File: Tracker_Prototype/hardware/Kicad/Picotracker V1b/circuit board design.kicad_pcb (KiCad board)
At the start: 2 copper layers, 47.4 x 20.1 mm, 55 parts, among them IC7 SPV1040, J1 Conn_01x06, J2 GND, J3 +SOL, J4 BATT_V+, J5 BATT_GND, J6 ICSS LOGO, Q1 Q_PMOS_DGS, SW1 SW_Push, U2 TPS62740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

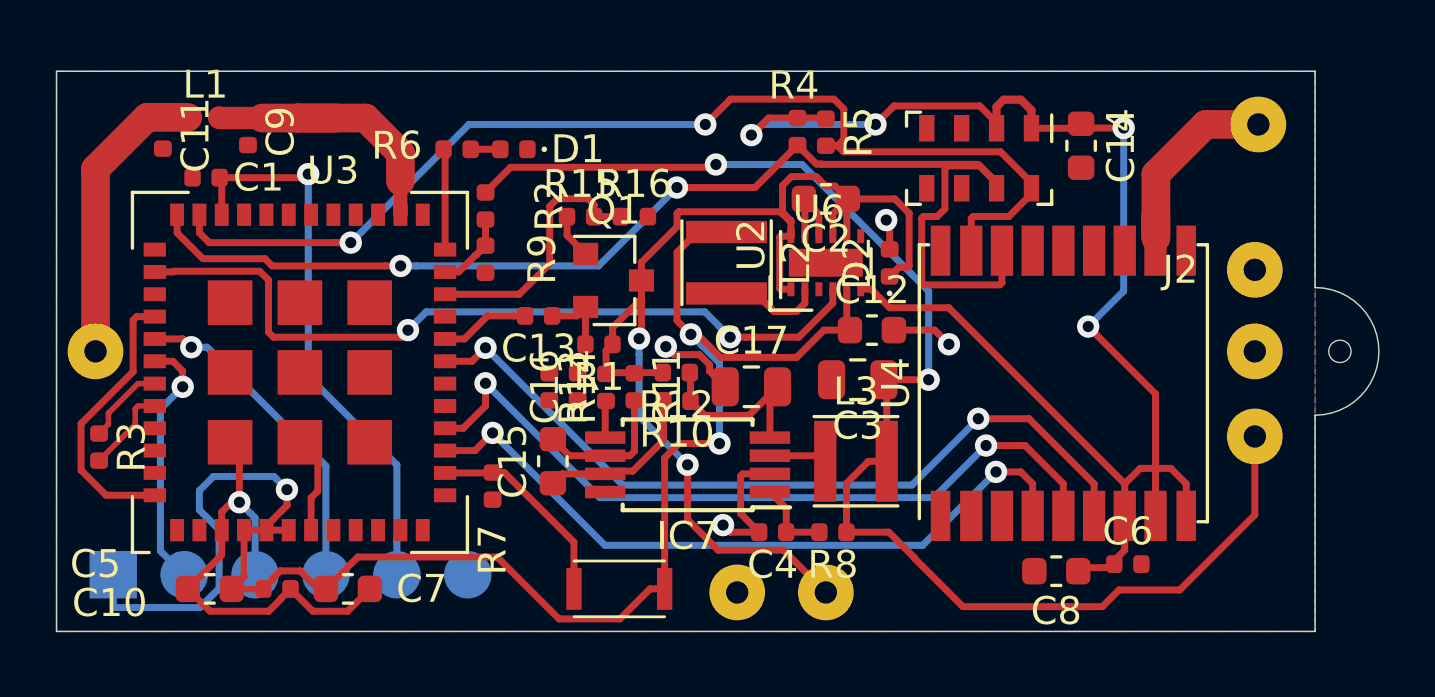
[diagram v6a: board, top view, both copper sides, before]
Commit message: Finished the layout of both the a and b variants. Silkscreen also done
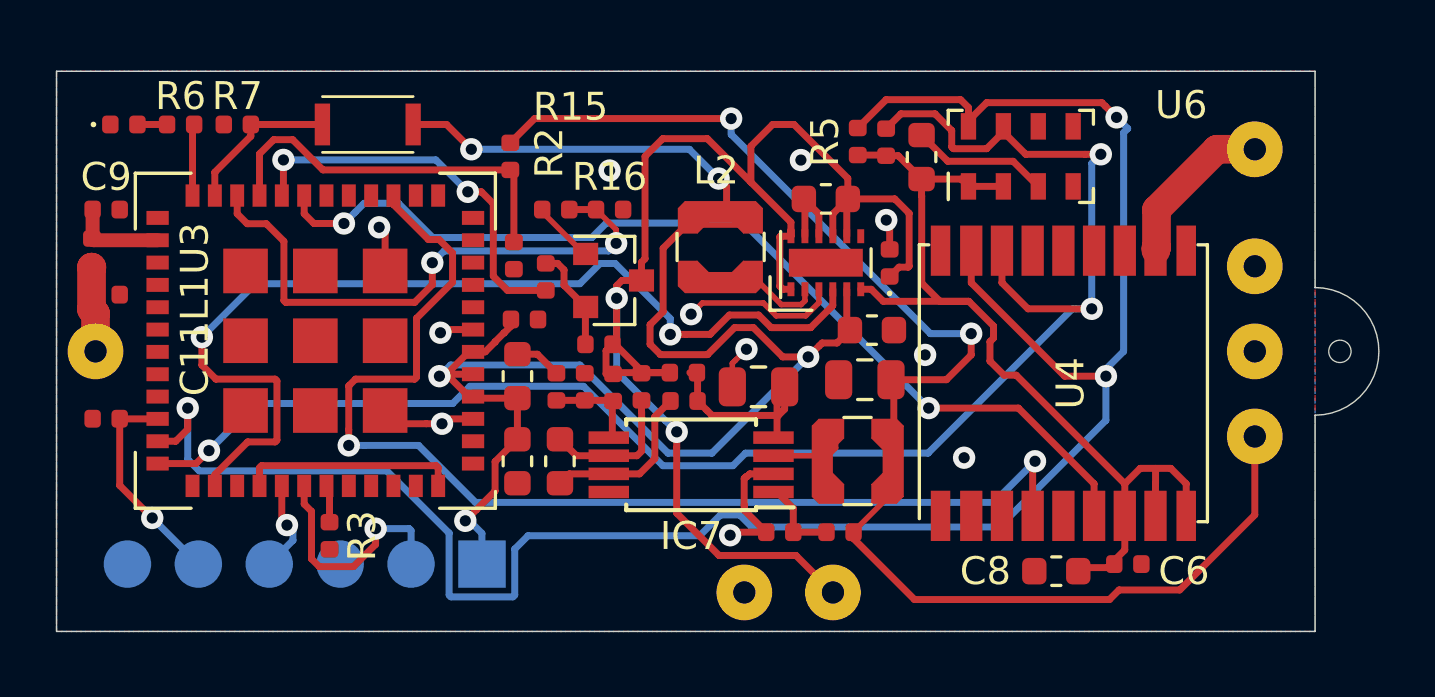
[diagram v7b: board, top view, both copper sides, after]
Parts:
- L2, L3: footprint Inductor_SMD:L_Taiyo-Yuden_NR-30xx -> flight-computer:L_Coilcraft_LPS3015
- moved SW1 18.9 mm to (277.4, 161.9)
- moved R7 15.9 mm to (273.2, 161.9), turned to 180 degrees
- moved D1 14.0 mm to (269.1, 161.9), turned to 0 degrees
- moved J1 13.2 mm to (281.9, 177.7), turned to 90 degrees
- moved C5 13.1 mm to (283.5, 168.9)
- moved C10 11.9 mm to (283.2, 174.0), turned to 270 degrees
- moved R6 9.95 mm to (271.1, 161.9), turned to 0 degrees
- moved C7 9.74 mm to (283.2, 170.9), turned to 90 degrees
- moved C1 9.35 mm to (268.5, 172.5)
- moved R3 8.84 mm to (276.5, 176.7)
- moved J6 7.92 mm to (288.0, 164.8)
- moved L1 6.31 mm to (268.0, 166.5), turned to 90 degrees
- moved C11 6.07 mm to (268.5, 168.0), turned to 0 degrees
- moved C9 5.80 mm to (268.5, 165.0), turned to 0 degrees
- moved C14 5.73 mm to (297.7, 163.1), turned to 90 degrees
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- renumbered J3 to +SOL, J2 to GND
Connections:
- U3 pad 14: /SWITCH -> (no net)
- U3 pad 16: /GPS_EXTINT -> (no net)
- U3 pad 21: (no net) -> /SOLAR_VOLTS
- U3 pad 23: /SOLAR_VOLTS -> /SWITCH
- U4 pad 5: /GPS_EXTINT -> (no net)
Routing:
- net /I2C1_SCL: track 39.6 -> 73.9 mm, vias 2 -> 3
- net /GPS_EXTINT: track 27.5 -> 0.00 mm, vias 2 -> 0
- net SENSOR_VCC: track 54.5 -> 34.6 mm, vias 4 -> 0
- net /GPS_TIMEPULSE: track 25.4 -> 40.9 mm
- net /I2C1_SDA: track 44.0 -> 58.1 mm, vias 2 -> 3
- net /RESET: track 20.3 -> 7.73 mm
- net /BATT_VOLTS: track 9.42 -> 20.8 mm, vias 0 -> 2
- net /SOLAR_VOLTS: track 2.77 -> 13.8 mm
- net /BATT_PWR_MEASURE: track 3.21 -> 14.2 mm, vias 0 -> 2
- net +BATT: track 44.6 -> 53.3 mm
- net /SWDIO: track 12.0 -> 3.32 mm
- net GND: track 37.5 -> 28.9 mm, vias 5 -> 11
- net Net-(C9-Pad1): track 11.0 -> 3.42 mm
- net Net-(AE1-Pad1): track 10.6 -> 3.09 mm
- net /SENSOR_EN: track 28.1 -> 35.6 mm
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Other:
- rule trace_min: 0.15 -> 0
- board text added: "PicoTracker LoRa V1b Imperial College Space Society Medad Newman, Richard Ibbotson"
- board text removed: "PicoTracker LoRa Imperial College Space Society Medad Newman, Richard Ibbotson"

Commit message: Ready to send for manufacturing
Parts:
- renumbered J4 to +BATT, J5 to GND
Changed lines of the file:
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@@
   (layers
     (0 F.Cu signal)
-    (31 B.Cu signal)
+    (31 B.Cu signal hide)
     (32 B.Adhes user)
     (33 F.Adhes user)
@@
     (tags connector)
     (attr virtual)
-    (fp_text reference J5 (at 0 -2.54 -90) (layer B.SilkS)
+    (fp_text reference GND (at 0.889 -2.54 -90) (layer B.SilkS)
       (effects (font (size 1 1) (thickness 0.15)) (justify mirror))
     )
@@
     (tags connector)
     (attr virtual)
-    (fp_text reference J4 (at 0 2.54 -90) (layer B.SilkS)
+    (fp_text reference +BATT (at 1.143 2.413 -90) (layer B.SilkS)
       (effects (font (size 1 1) (thickness 0.15)) (justify mirror))
     )
